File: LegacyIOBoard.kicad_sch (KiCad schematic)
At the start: 152 parts, among them J1 350826-1, J10 AFBR-59R5LZ, J11 AFBR-59R5LZ, J12 AFBR-59R5LZ, J13 AFBR-59R5LZ, J14 10845031, J15 10845031, J16 10845031, J17 10845031, J18 10845031, J19 10845031, J2 A_In, J20 10845031, J21 10845031, J22 678005005, J23 678005005, J24 A_In, J25 A_Out, J26 678005005, J27 678005005, J28 A_In, J29 A_Out, J3 A_Out, J31 B08B-PASKLFSN, J4 678005005, J5 678005005, J6 A_In, J7 A_Out, J8 678005005, J9 678005005, K1 PR23-12V-900-1C, K10 PR23-12V-900-1C, K11 G5LE-1-VD-DC12, K2 PR23-12V-900-1C, K3 PR23-12V-900-1C, K4 HE722A1200, K5 HE722A1200, K6 HE722A1200, K7 HE722A1200, K9 G5LE-1-VD-DC12, U1 AP62300TWU-7, U10 DMN3023L-7, U11 DMN3023L-7, U12 SFH615A-4X009, U13 DMN3023L-7, U14 SFH615A-4X009, U15 DMN3023L-7, U16 SFH615A-4X009, U17 DMN3023L-7, U18 AP3211KTR-G1, U3 SC0192_9_, U4 DMN3023L-7, U5 DMN3023L-7, U6 DMN3023L-7, U7 DMN3023L-7, U8 DMN3023L-7, U9 SFH615A-4X009

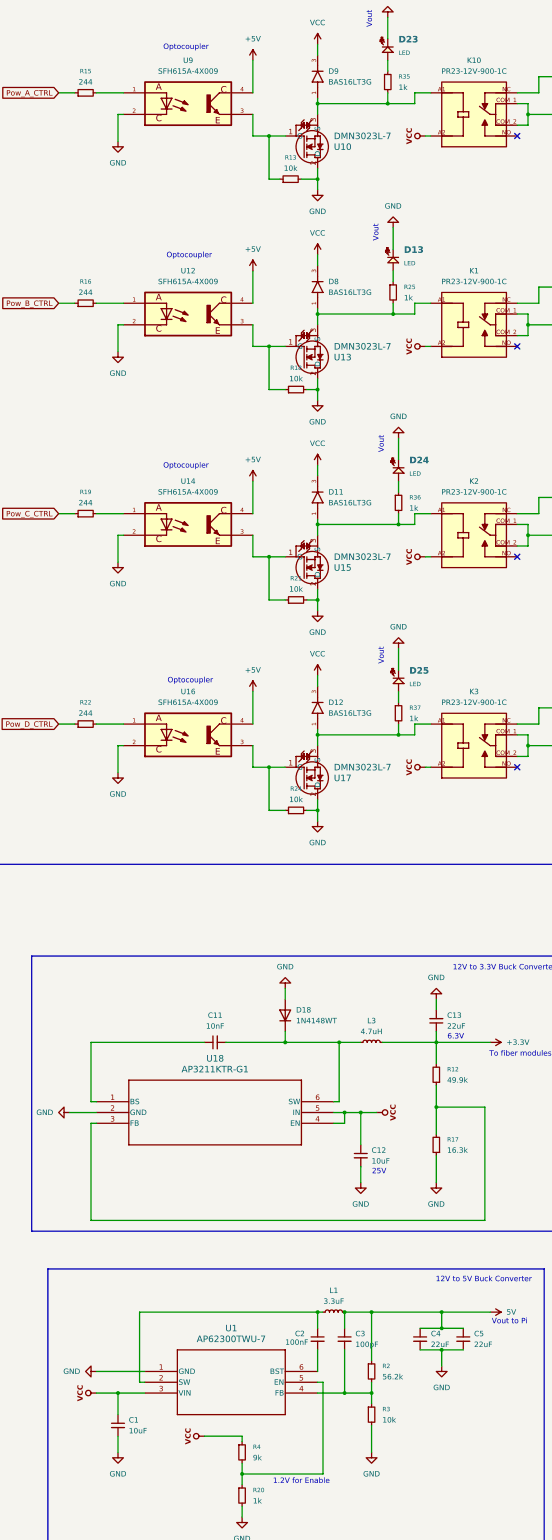
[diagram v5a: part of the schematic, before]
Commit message: Ref #6 Added some Dak part numbers to the BOM.
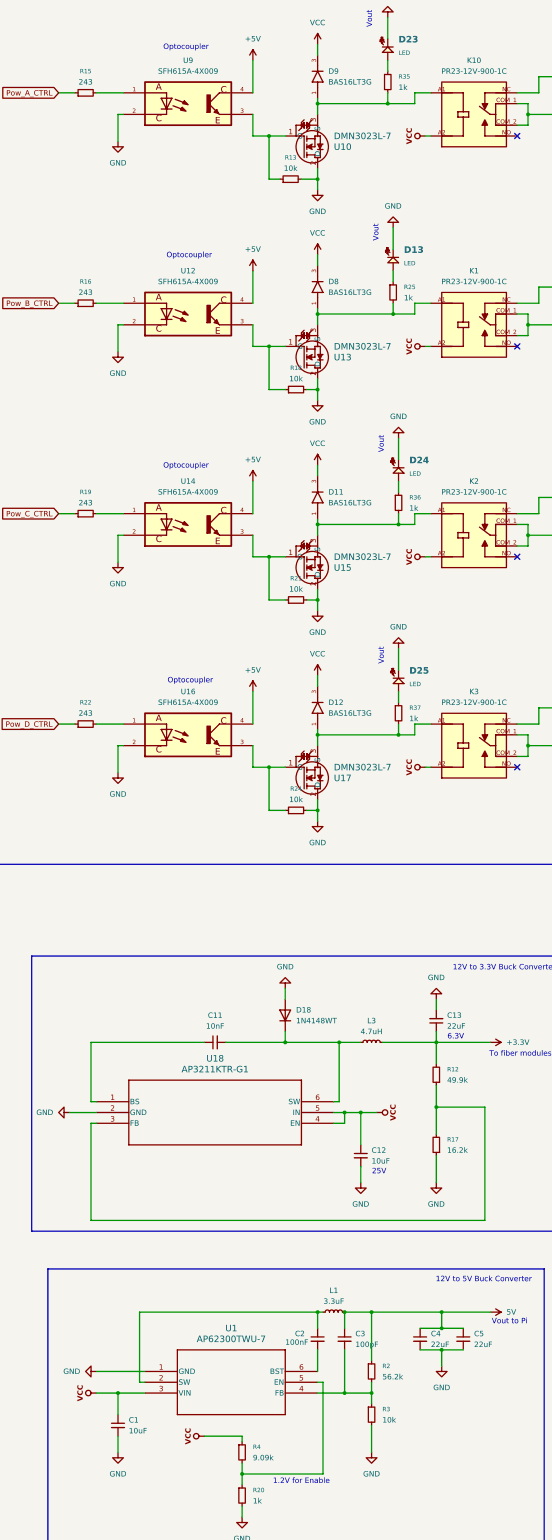
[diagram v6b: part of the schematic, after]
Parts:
- R15, R16, R19, R22: value 244 -> 243
- R17: value 16.3k -> 16.2k
- R4: value 9k -> 9.09k
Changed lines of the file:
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@@
 			)
 		)
-		(property "Value" "244"
+		(property "Value" "243"
 			(at 237.49 193.04 90)
 			(effects
@@
 			)
 		)
-		(property "Value" "16.3k"
+		(property "Value" "16.2k"
 			(at 322.58 295.9099 0)
 			(effects
@@
 			)
 		)
-		(property "Value" "244"
+		(property "Value" "243"
 			(at 237.49 44.45 90)
 			(effects
@@
 			)
 		)
-		(property "Value" "244"
+		(property "Value" "243"
 			(at 237.49 93.98 90)
 			(effects
@@
 			)
 		)
-		(property "Value" "244"
+		(property "Value" "243"
 			(at 237.49 143.51 90)
 			(effects
@@
 			)
 		)
-		(property "Value" "9k"
+		(property "Value" "9.09k"
 			(at 276.86 368.2999 0)
 			(effects

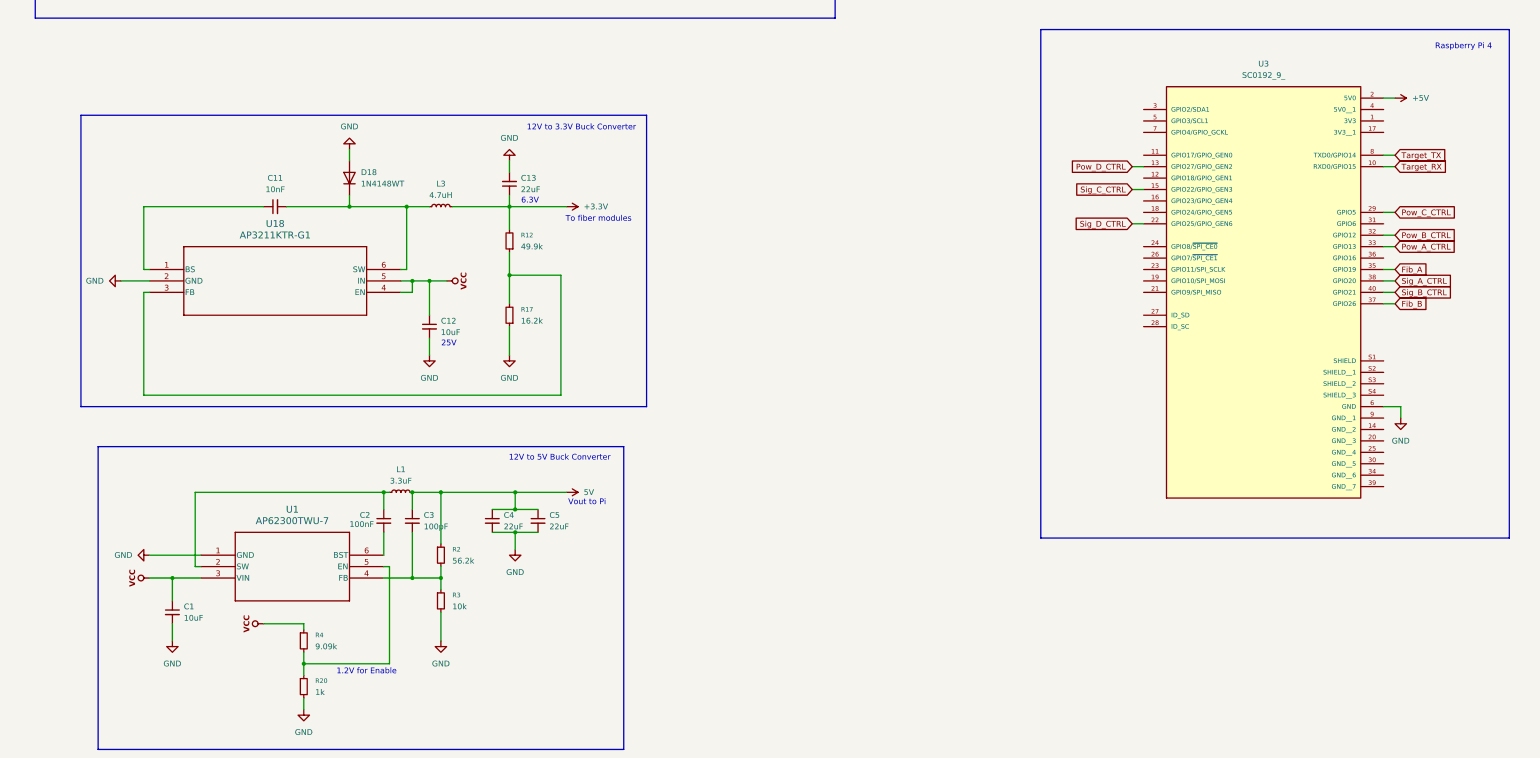
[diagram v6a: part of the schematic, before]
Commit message: Ref 7 Changed 3.3V buck converter to the same IC as the 5V buck. Switched TX and RX on the Pi. Corrected typo on inductor.
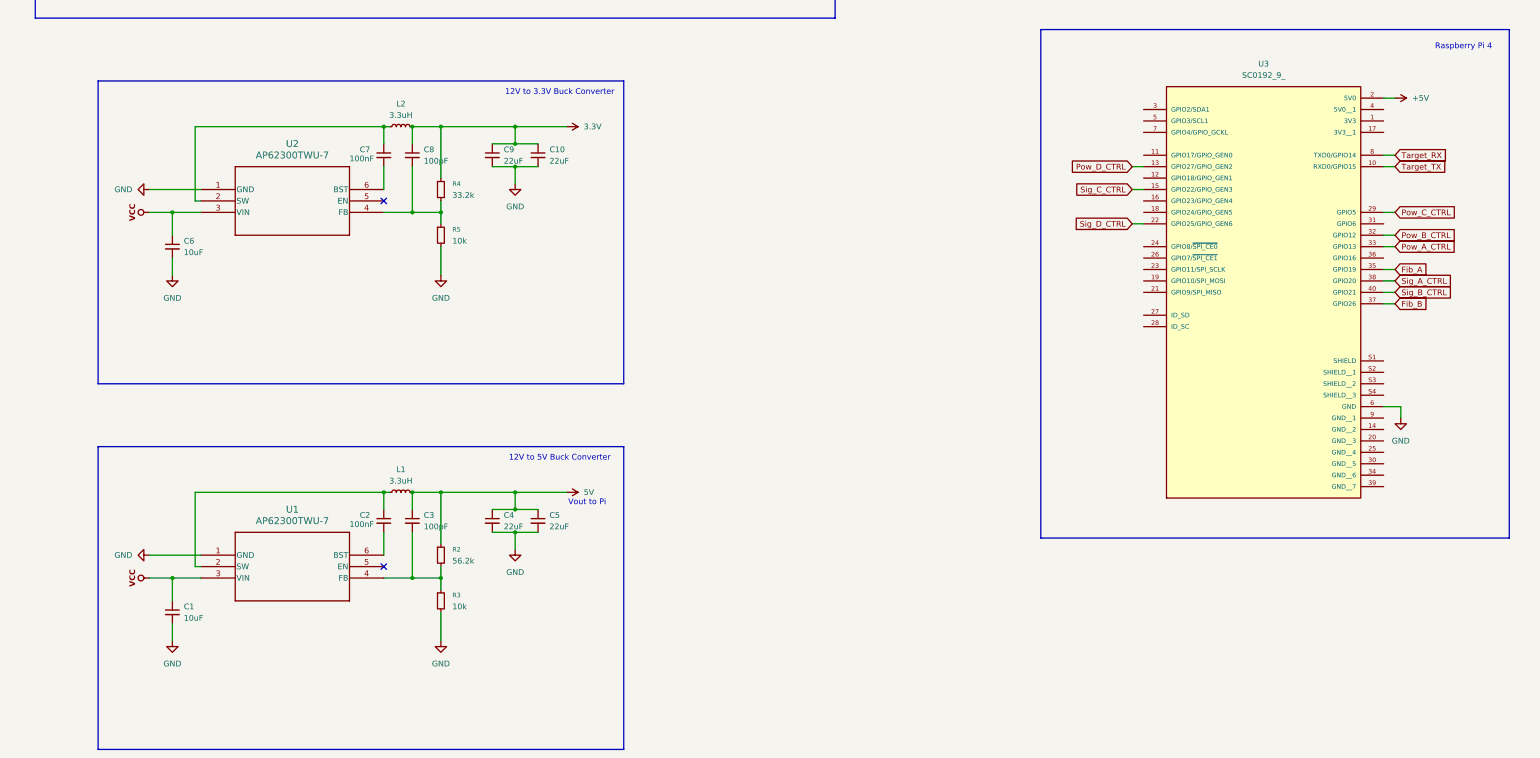
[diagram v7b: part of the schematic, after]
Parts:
- removed C11: 10nF, symbol Device:C_Small
- removed C12: 10uF, symbol Device:C_Small
- removed C13: 22uF, symbol Device:C_Small
- removed D18: 1N4148WT, Diode_SMD:D_SOD-523, symbol Diode:1N4148WT
- removed L3: 4.7uH, symbol Device:L_Small
- removed R12: 49.9k, symbol Device:R_Small
- removed R17: 16.2k, symbol Device:R_Small
- removed R20: 1k, symbol Device:R_Small
- removed U18: AP3211KTR-G1, SOT23-6_DIO, symbol 2025-06-13_17-05-22:AP3211KTR-G1
- added C10, C9: 22uF, symbol Device:C_Small
- added C6: 10uF, symbol Device:C_Small
- added C7: 100nF, symbol Device:C_Small
- added C8: 100pF, symbol Device:C_Small
- added L2: 3.3uH, symbol Device:L_Small
- added R5: 10k, symbol Device:R_Small
- added U2: AP62300TWU-7, TSOT26-WU_DIO, symbol 2025-06-23_15-31-30:AP62300TWU-7
- L1: value 3.3uF -> 3.3uH
- R4: value 9.09k -> 33.2k
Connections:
- net GND: now also C10.2, C6.2, C9.2, R5.2, U2.1 (GND)
- net Target_RX: now also U3.8 (TXD0/GPIO14); no longer U3.10 (RXD0/GPIO15)
- net Target_TX: now also U3.10 (RXD0/GPIO15); no longer U3.8 (TXD0/GPIO14)
- net VCC: now also C6.1, U2.3 (VIN); no longer R4.1
- net at U1.5 (EN): no longer R4.2
- new net: C7.1, L2.1, U2.2 (SW)
- new net: C7.2, U2.6 (BST)
- new net: C8.2, R4.2, R5.1, U2.4 (FB)
- new net 3.3V: C10.1, C8.1, C9.1, L2.2, R4.1
- no-connect marks 45 -> 47
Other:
- note removed: "1.2V for Enable"
- note removed: "25V"
- note removed: "6.3V"
- note removed: "To fiber modules"

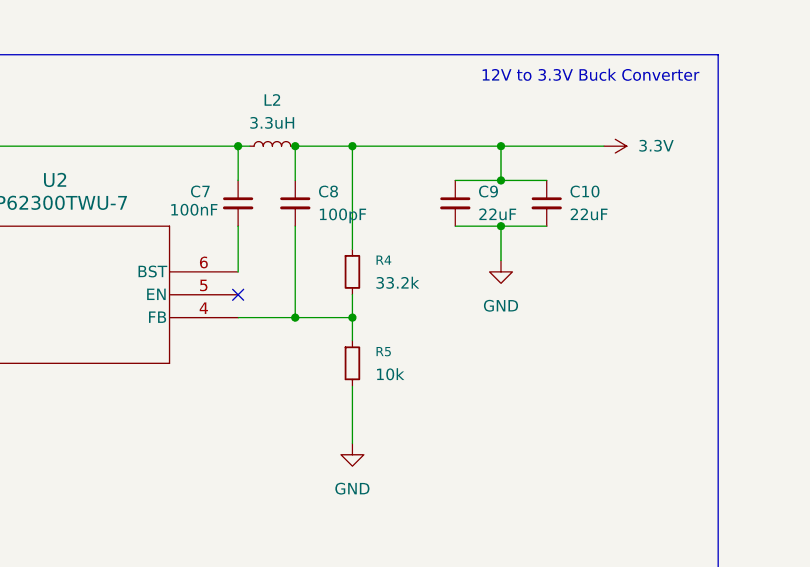
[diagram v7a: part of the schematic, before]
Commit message: Made change to R4 to reflect part availability.
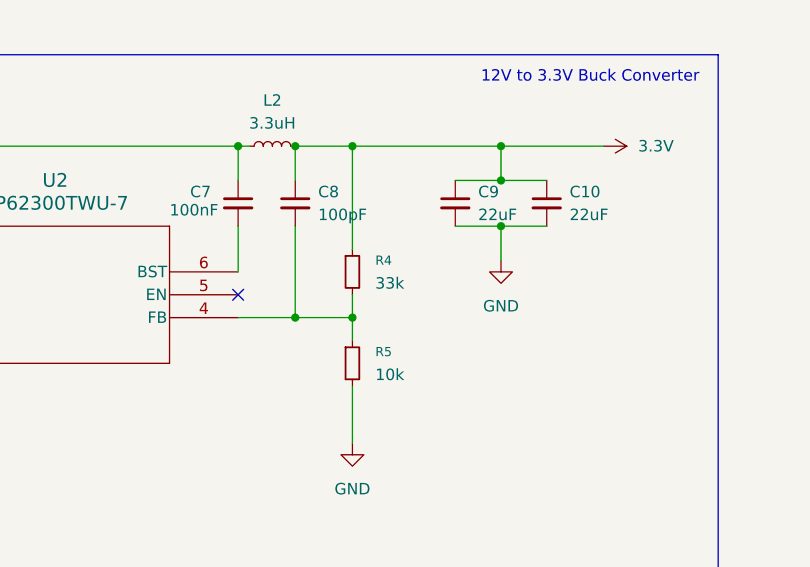
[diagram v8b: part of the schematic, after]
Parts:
- R4: value 33.2k -> 33k
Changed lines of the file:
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@@
 			)
 		)
-		(property "Value" "33.2k"
+		(property "Value" "33k"
 			(at 307.34 267.9699 0)
 			(effects
